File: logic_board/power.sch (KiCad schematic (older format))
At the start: 21 parts, among them J4 Amphenol 124015, J5 Batt, SW5 Power, U4 TPS562200, U5 BQ24090DGQR

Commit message: Add a JST battery connector
The bare solder pads made me a bit nervous wrt the risk of shorting
the battery. Uses 2mm JST connector, which seems to be a common battery
connector.
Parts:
- J5: footprint custom_footprints:Solder Pads 2x1 -> custom_footprints:JST PH HEADER SMD 2POS 2MM
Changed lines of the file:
@@
 F 0 "J5" H 9030 1942 50  0000 L CNN
 F 1 "Batt" H 9030 1851 50  0000 L CNN
-F 2 "custom_footprints:Solder Pads 2x1" H 8950 1950 50  0001 C CNN
+F 2 "custom_footprints:JST PH HEADER SMD 2POS 2MM" H 8950 1950 50  0001 C CNN
 F 3 "~" H 8950 1950 50  0001 C CNN
 	1    8950 1950

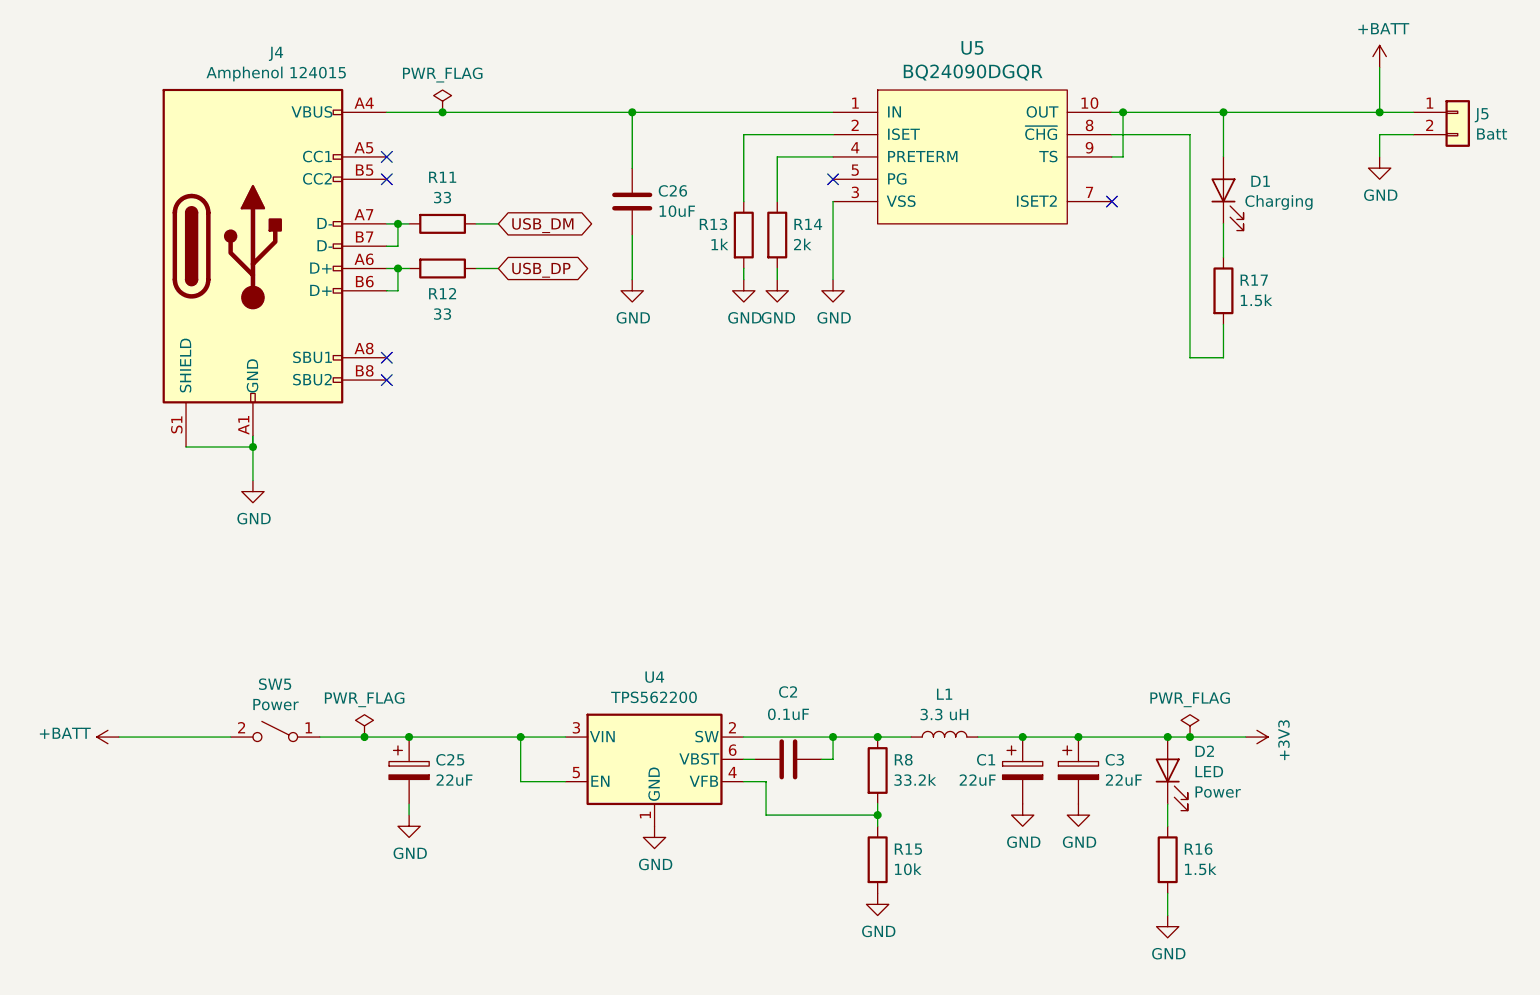
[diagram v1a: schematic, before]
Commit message: Re-layout for the third time
In general, tried to make things a bit cleaner. Also:
- Needed to add a capacitor on charger output.
- Use a footprint with copper pad under charger for heat dissipation
- Use through-hole LEDs, which are easier to bend 90 degrees to poke out
  the sides of the case.
- I read about a trick: put all power supply bypass caps under the IC, which
  saves space.
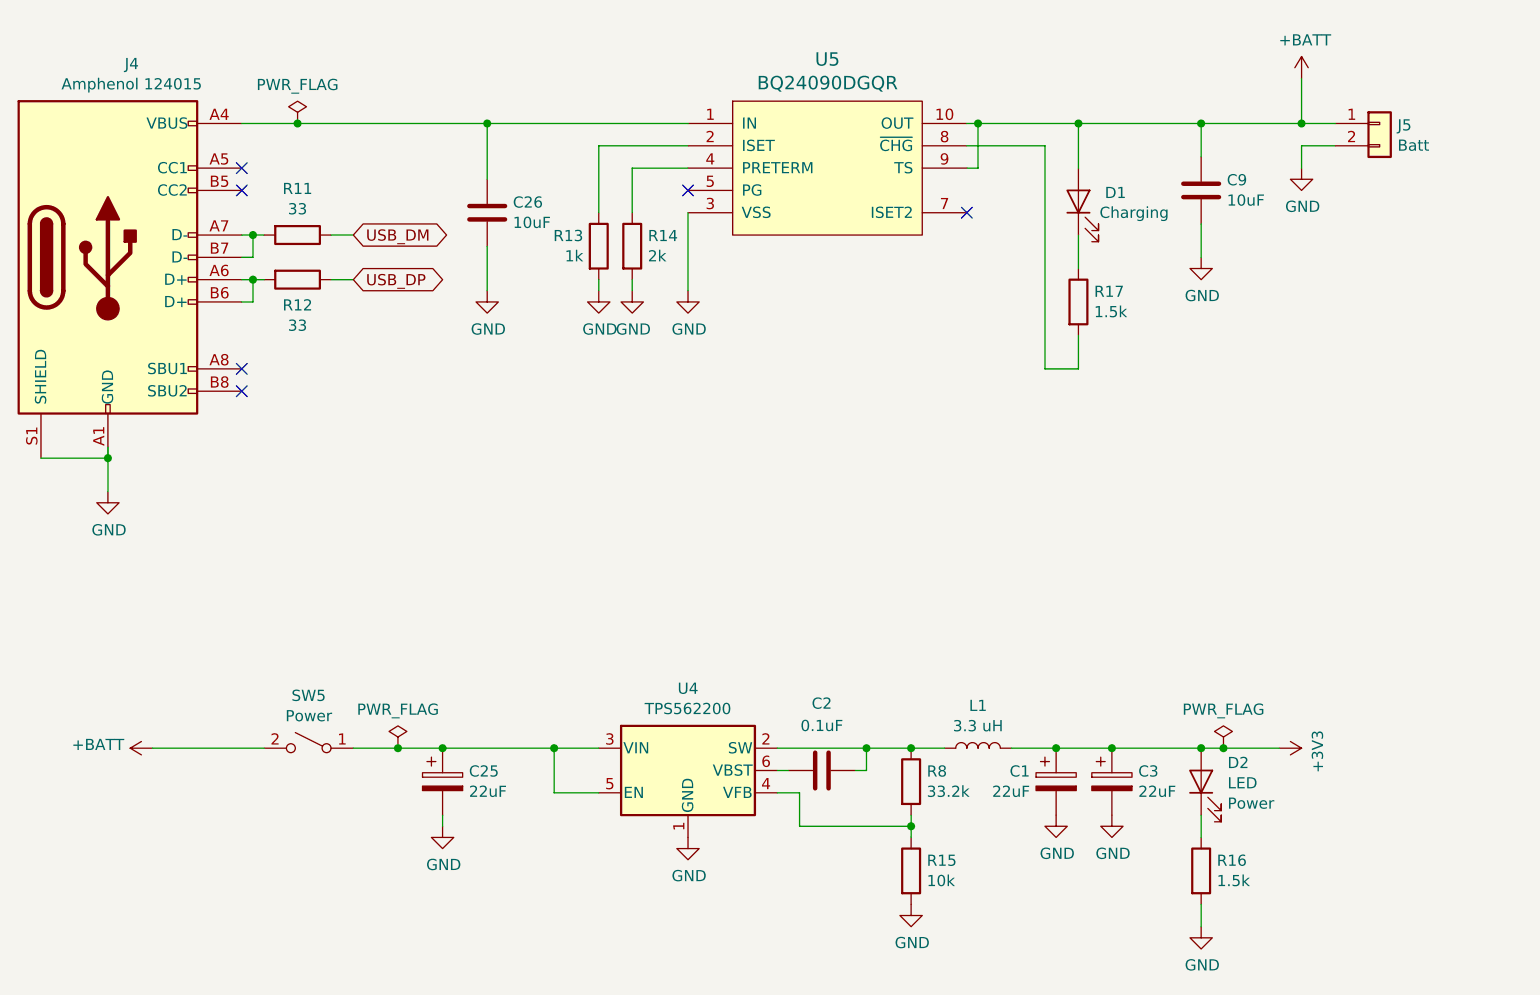
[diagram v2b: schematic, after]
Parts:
- added C9: 10uF, Capacitors_SMD:C_0402, symbol Device:C
- D1, D2: footprint LEDs:LED_0402 -> LEDs:LED_D3.0mm
- U5: footprint Housings_SSOP:MSOP-10_3x3mm_Pitch0.5mm -> Housings_SSOP:MSOP-10-1EP_3x3mm_Pitch0.5mm
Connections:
- net +BATT: now also C9.1
- net GND: now also C9.2
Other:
- moved on the sheet: C1, C2, C25, C26, C3, D1, D2, J4, J5, L1, R11, R12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

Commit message: Update BOM
Move power/charge LEDs back from edge so there's enough room. Use horizontal footprint.
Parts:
- D1, D2: footprint LEDs:LED_D3.0mm -> LEDs:LED_D3.0mm_Horizontal_O1.27mm_Z2.0mm
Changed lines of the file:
@@
 F 0 "D1" V 7289 2232 50  0000 R CNN
 F 1 "LED" V 7198 2232 50  0001 R CNN
-F 2 "LEDs:LED_D3.0mm" H 7250 2350 50  0001 C CNN
+F 2 "LEDs:LED_D3.0mm_Horizontal_O1.27mm_Z2.0mm" H 7250 2350 50  0001 C CNN
 F 3 "~" H 7250 2350 50  0001 C CNN
 F 4 "Charging" V 7200 2100 50  0000 C CNN "Name"
@@
 F 0 "D2" V 7884 4832 50  0000 R CNN
 F 1 "LED" V 7793 4832 50  0000 R CNN
-F 2 "LEDs:LED_D3.0mm" H 7800 4950 50  0001 C CNN
+F 2 "LEDs:LED_D3.0mm_Horizontal_O1.27mm_Z2.0mm" H 7800 4950 50  0001 C CNN
 F 3 "~" H 7800 4950 50  0001 C CNN
 F 4 "Power" V 7702 4832 50  0000 R CNN "Name"

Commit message: Switch to a microcontroller with more SRAM
This is necessary to enable some effects like reverb and echo.
This part has a similar pinout, but not exactly the same, which required some layout
changes.
I also took this opportuntity to move the serial pins to a separate header with its
own ground, which makes connecting a serial debugger and SWD interface at the same
time easier.
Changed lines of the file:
@@
 Sheet 4 4
 Title "Power"
-Date "2020-02-02"
-Rev "1.0"
+Date "2020-02-08"
+Rev "1.1"
 Comp ""
 Comment1 ""
@@
 	7800 5100 7800 5200
 Wire Wire Line
-	7800 5500 7800 5600
-Wire Wire Line
 	2600 3500 2900 3500
 Wire Wire Line
@@
 Wire Wire Line
 	7800 2600 7800 2450
+Wire Wire Line
+	7800 5500 7800 5550
+$Comp
+L power:PWR_FLAG #FLG0102
+U 1 1 5E598B20
+P 7600 5450
+F 0 "#FLG0102" H 7600 5525 50  0001 C CNN
+F 1 "PWR_FLAG" H 7600 5623 50  0000 C CNN
+F 2 "" H 7600 5450 50  0001 C CNN
+F 3 "~" H 7600 5450 50  0001 C CNN
+	1    7600 5450
+	1    0    0    -1
+$EndComp
+Wire Wire Line
+	7800 5550 7600 5550
+Wire Wire Line
+	7600 5550 7600 5450
+Connection ~ 7800 5550
+Wire Wire Line
+	7800 5550 7800 5600
 $EndSCHEMATC

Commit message: Add pulldown resistors on CC1 and CC2 pins to enable VBUS power
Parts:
- added R1, R2: 5.1k, Resistors_SMD:R_0402, symbol Device:R
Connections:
- net GND: now also R1.1, R2.2
- net at J4.A5 (CC1): now also R1.2
- net at J4.B5 (CC2): now also R2.1
- no-connect marks 6 -> 4
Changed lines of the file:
@@
 	6800 2000 7250 2000
 Connection ~ 6800 2000
-NoConn ~ 3500 2200
-NoConn ~ 3500 2300
 NoConn ~ 3500 3100
 NoConn ~ 3500 3200
@@
 Wire Wire Line
 	7800 5550 7800 5600
+$Comp
+L Device:R R1
+U 1 1 5E403BD3
+P 4000 2200
+F 0 "R1" V 3900 2150 50  0000 C CNN
+F 1 "5.1k" V 3900 2300 50  0000 C CNN
+F 2 "Resistors_SMD:R_0402" V 3930 2200 50  0001 C CNN
+F 3 "~" H 4000 2200 50  0001 C CNN
+	1    4000 2200
+	0    1    1    0
+$EndComp
+$Comp
+L Device:R R2
+U 1 1 5E40452A
+P 4000 2300
+F 0 "R2" V 3900 2350 50  0000 C CNN
+F 1 "5.1k" V 3900 2200 50  0000 C CNN
+F 2 "Resistors_SMD:R_0402" V 3930 2300 50  0001 C CNN
+F 3 "~" H 4000 2300 50  0001 C CNN
+	1    4000 2300
+	0    -1   -1   0
+$EndComp
+$Comp
+L power:GND #PWR06
+U 1 1 5E405DA3
+P 4250 2200
+F 0 "#PWR06" H 4250 1950 50  0001 C CNN
+F 1 "GND" V 4255 2072 50  0000 R CNN
+F 2 "" H 4250 2200 50  0001 C CNN
+F 3 "" H 4250 2200 50  0001 C CNN
+	1    4250 2200
+	0    -1   -1   0
+$EndComp
+$Comp
+L power:GND #PWR08
+U 1 1 5E406767
+P 4250 2300
+F 0 "#PWR08" H 4250 2050 50  0001 C CNN
+F 1 "GND" V 4255 2172 50  0000 R CNN
+F 2 "" H 4250 2300 50  0001 C CNN
+F 3 "" H 4250 2300 50  0001 C CNN
+	1    4250 2300
+	0    -1   -1   0
+$EndComp
+Wire Wire Line
+	3500 2200 3850 2200
+Wire Wire Line
+	3500 2300 3850 2300
+Wire Wire Line
+	4150 2200 4250 2200
+Wire Wire Line
+	4150 2300 4250 2300
 $EndSCHEMATC

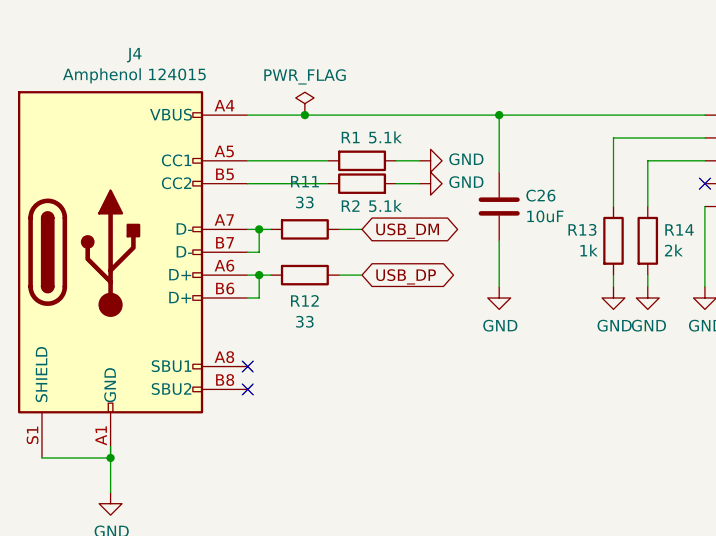
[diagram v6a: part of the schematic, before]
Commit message: Remove USB series termination resistors
Page 179 of the datasheet states: "No external termination series
resistors are required on USB_PD P(D+) and USB_DM (D-); the matching
impedance is already included in the embedded driver." (There's a typo,
presumably they meant USB_DP).
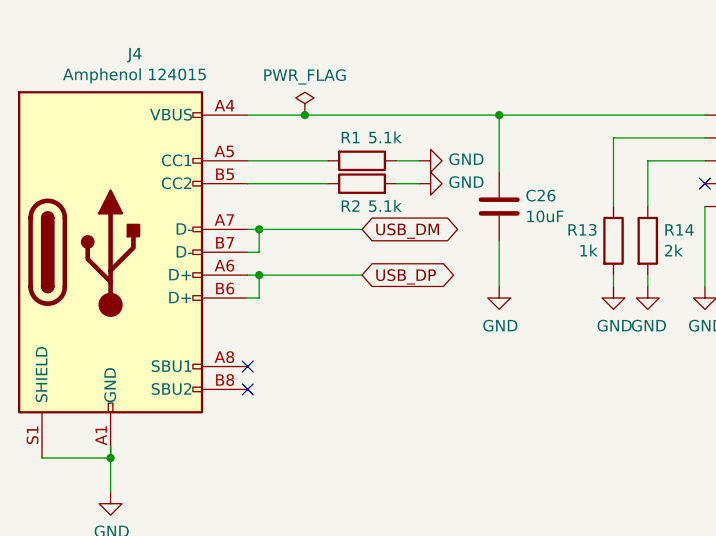
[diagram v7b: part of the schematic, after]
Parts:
- removed R11, R12: 33, Resistors_SMD:R_0402, symbol Device:R
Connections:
- net USB_DM: now also J4.A7 (D-), J4.B7 (D-)
- net USB_DP: now also J4.A6 (D+), J4.B6 (D+)
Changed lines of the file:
@@
 Text GLabel 4000 2700 2    50   BiDi ~ 0
 USB_DP
-$Comp
-L Device:R R11
-U 1 1 5E4A45C0
-P 3750 2500
-F 0 "R11" V 3543 2500 50  0000 C CNN
-F 1 "33" V 3634 2500 50  0000 C CNN
-F 2 "Resistors_SMD:R_0402" V 3680 2500 50  0001 C CNN
-F 3 "~" H 3750 2500 50  0001 C CNN
-	1    3750 2500
-	0    1    1    0
-$EndComp
-$Comp
-L Device:R R12
-U 1 1 5E4A4FEC
-P 3750 2700
-F 0 "R12" V 3865 2700 50  0000 C CNN
-F 1 "33" V 3956 2700 50  0000 C CNN
-F 2 "Resistors_SMD:R_0402" V 3680 2700 50  0001 C CNN
-F 3 "~" H 3750 2700 50  0001 C CNN
-	1    3750 2700
-	0    1    1    0
-$EndComp
 Wire Wire Line
 	3500 2500 3550 2500
 Wire Wire Line
 	3500 2700 3550 2700
-Wire Wire Line
-	3900 2500 4000 2500
-Wire Wire Line
-	3900 2700 4000 2700
 Wire Wire Line
 	3500 2600 3550 2600
@@
 Connection ~ 3550 2500
 Wire Wire Line
-	3550 2500 3600 2500
-Wire Wire Line
 	3500 2800 3550 2800
 Wire Wire Line
 	3550 2800 3550 2700
 Connection ~ 3550 2700
-Wire Wire Line
-	3550 2700 3600 2700
 $Comp
 L Device:R R14
@@
 Wire Wire Line
 	4150 2300 4250 2300
+Wire Wire Line
+	3550 2500 4000 2500
+Wire Wire Line
+	3550 2700 4000 2700
 $EndSCHEMATC
